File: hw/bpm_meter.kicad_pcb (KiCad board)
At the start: 2 copper layers, 55 x 73.5 mm, 78 parts, among them J1 Conn_01x05_Pin, J2 Conn_01x03_Pin, J901 USB_C_Receptacle_USB2.0, Q1 AO3400A, SW901 SW_MEC_5E, U1 SLS0391FR1A1GD, U2 AOZ1282CI, U3 H11L1, U4 SLS0391FR1A1GD, U5 SLS0391FR1A1GD, U6 LP5030, U7 AMS1117-3.3, U901 RP2040, U902 AMS1117-3.3, U903 W25Q128JVS, Y901 Crystal_GND24_Small

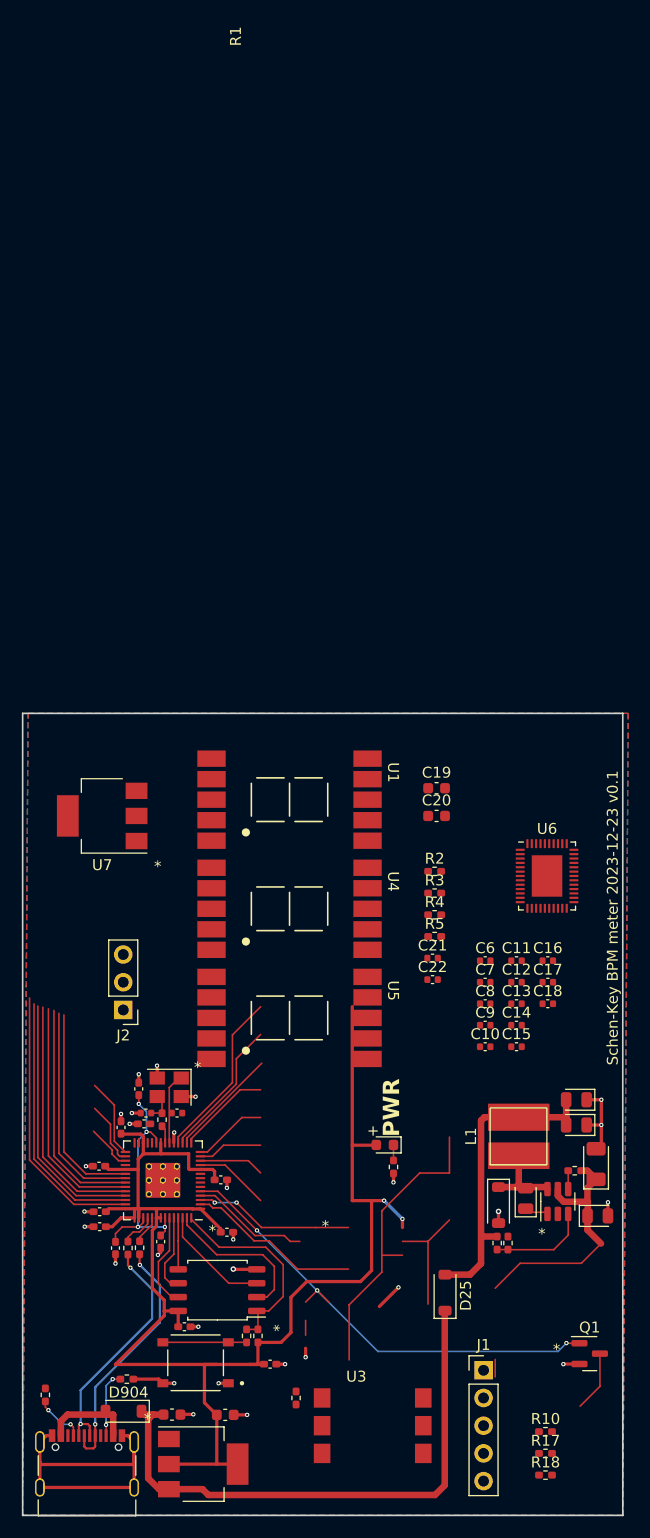
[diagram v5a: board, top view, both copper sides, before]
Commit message: Removed unused tracks, did some prearrangement of components
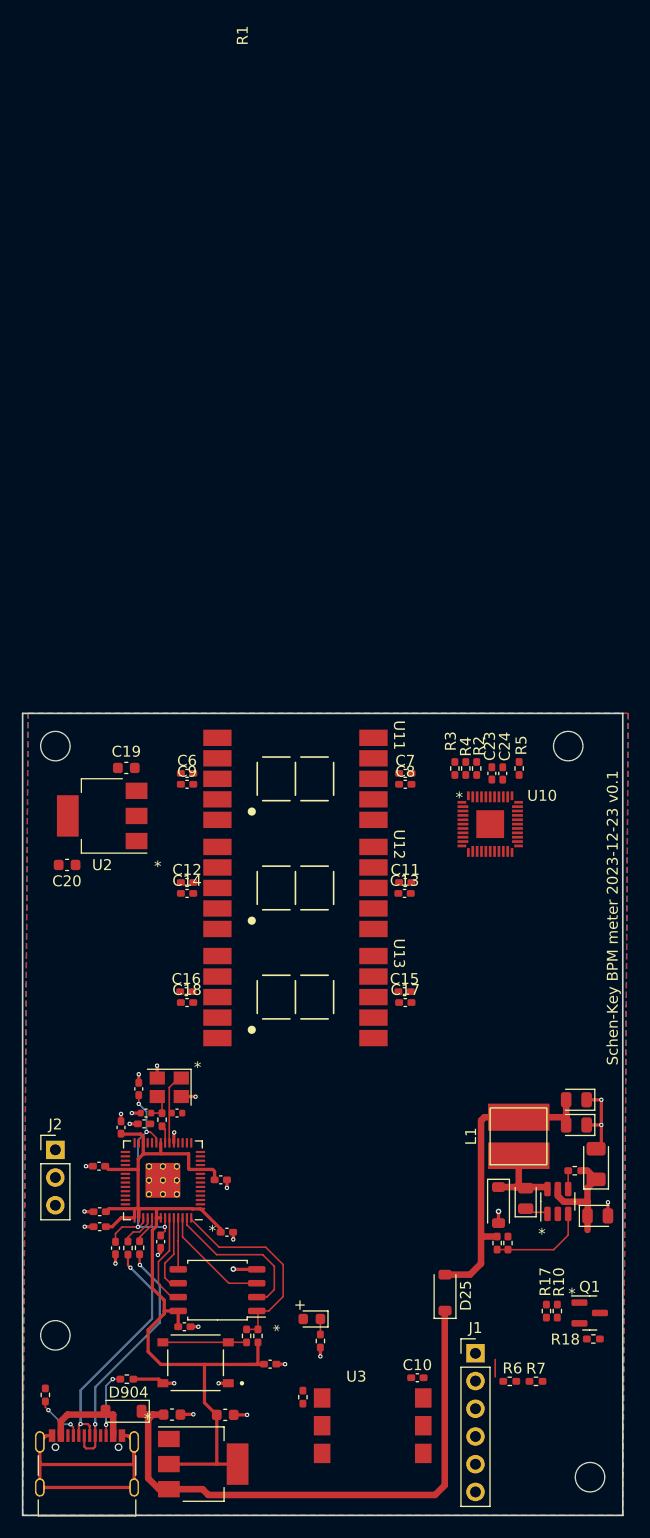
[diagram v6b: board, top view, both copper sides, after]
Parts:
- removed C21, C22: 1u, Capacitor_SMD:C_0402_1005Metric
- removed U6: LP5030, Package_DFN_QFN:VQFN-46-1EP_5x6mm_P0.4mm_EP2.8x3.8mm
- added C23: 1u, Capacitor_SMD:C_0402_1005Metric_Pad0.74x0.62mm_HandSolder, F.Cu at (117.0, 64.5)
- added C24: 100n, Capacitor_SMD:C_0402_1005Metric_Pad0.74x0.62mm_HandSolder, F.Cu at (118.0, 64.5)
- added H1: MountingHole, MountingHole:MountingHole_2.7mm_M2.5, F.Cu at (77.0, 62.0)
- added H2: MountingHole, MountingHole:MountingHole_2.7mm_M2.5, F.Cu at (124.0, 62.0)
- added H3: MountingHole, MountingHole:MountingHole_2.7mm_M2.5, F.Cu at (126.0, 129.0)
- added H4: MountingHole, MountingHole:MountingHole_2.7mm_M2.5, F.Cu at (77.0, 116.0)
- added R6: 10k, Resistor_SMD:R_0402_1005Metric_Pad0.72x0.64mm_HandSolder, F.Cu at (118.6, 120.2)
- added R7: 4k7, Resistor_SMD:R_0402_1005Metric_Pad0.72x0.64mm_HandSolder, F.Cu at (121.0, 120.2)
- added U10: IS31FL3236A, 00_project_library:QFN-44-5x5mm_P0.4mm, F.Cu at (116.8, 69.2)
- C10, C11, C12, C13, C14, C15, C16, C17, C18, C6, C7, C8, C9: footprint Capacitor_SMD:C_0402_1005Metric -> Capacitor_SMD:C_0402_1005Metric_Pad0.74x0.62mm_HandSolder
- J1: value Conn_01x05_Pin -> Conn_01x06_Pin; footprint Connector_PinHeader_2.54mm:PinHeader_1x05_P2.54mm_Vertical -> Connector_PinHeader_2.54mm:PinHeader_1x06_P2.54mm_Vertical
- R2: value 4k7 -> 7k5
- R5: value 4k7 -> 100k
- R901, R902: value 5.1K -> 5.1k
- R906: value 1K -> 1k
- R907: value 10K -> 10k
- moved C9 35.1 mm to (89.1, 65.5)
- moved C20 34.2 mm to (78.1, 72.9)
- moved C16 33.3 mm to (89.0, 84.5)
- moved C18 33.1 mm to (89.1, 85.5)
- moved C14 32.5 mm to (89.1, 75.5)
- moved C6 32.3 mm to (89.1, 64.5)
- moved C12 31.5 mm to (89.1, 74.5)
- moved C10 31.0 mm to (110.2, 119.9)
- moved C19 28.5 mm to (83.5, 64.0), turned to 180 degrees
- moved C8 21.4 mm to (109.1, 65.5)
- moved C7 20.5 mm to (109.1, 64.5)
- moved D901 17.3 mm to (100.5, 114.5)
- moved R905 17.3 mm to (101.3, 116.5)
- moved R5 17.2 mm to (119.5, 64.0), turned to 90 degrees
- moved C13 14.4 mm to (109.0, 75.5)
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- renumbered U2 to U1, U1 to U11, U4 to U12, U5 to U13, U7 to U2
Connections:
- net en renamed sdb
- J1 pad 5: GND -> Net-(J1-Pin_5)
- R1 pad 2: Net-(J1-Pin_3) -> Net-(J1-Pin_4)
- R17 pad 2: Net-(J1-Pin_2) -> Net-(J1-Pin_3)
- U3 pad 2: Net-(J1-Pin_4) -> Net-(J1-Pin_5)
- U901 pad 15: Net-(J2-Pin_1) -> unconnected-(U901-GPIO12-Pad15)
- U901 pad 16: Net-(J2-Pin_2) -> unconnected-(U901-GPIO13-Pad16)
- U901 pad 17: Net-(J2-Pin_3) -> unconnected-(U901-GPIO14-Pad17)
- U901 pad 38: unconnected-(U901-GPIO26/ADC0-Pad38) -> beat_adc
- U901 pad 39: unconnected-(U901-GPIO27/ADC1-Pad39) -> Net-(J2-Pin_1)
- U901 pad 40: unconnected-(U901-GPIO28/ADC2-Pad40) -> Net-(J2-Pin_2)
- U901 pad 41: unconnected-(U901-GPIO29/ADC3-Pad41) -> Net-(J2-Pin_3)
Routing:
- net +3V3: track 138.8 -> 85.4 mm, vias 2 -> 0
- net Net-(Q1-G): track 44.2 -> 0.00 mm, vias 3 -> 0
- net (no net): track 39.9 -> 0.00 mm
- net beat_od: track 26.5 -> 0.00 mm
- net unconnected-(U901-GPIO29/ADC3-Pad41): track 25.3 -> 0.00 mm
- net unconnected-(U901-GPIO28/ADC2-Pad40): track 24.2 -> 0.00 mm
- net unconnected-(U901-GPIO27/ADC1-Pad39): track 23.3 -> 0.00 mm
- net unconnected-(U901-GPIO26/ADC0-Pad38): track 22.6 -> 0.00 mm
- net beat_opto: track 21.7 -> 0.00 mm
- net unconnected-(U901-GPIO23-Pad35): track 19.9 -> 0.00 mm
- net unconnected-(U901-GPIO22-Pad34): track 19.0 -> 0.00 mm
- net sda: track 16.0 -> 0.00 mm
- net unconnected-(U901-GPIO15-Pad18): track 15.6 -> 0.00 mm
- net scl: track 14.6 -> 0.00 mm, vias 2 -> 0
- net +14V: track 25.0 -> 11.8 mm
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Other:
- board text removed: "PWR"

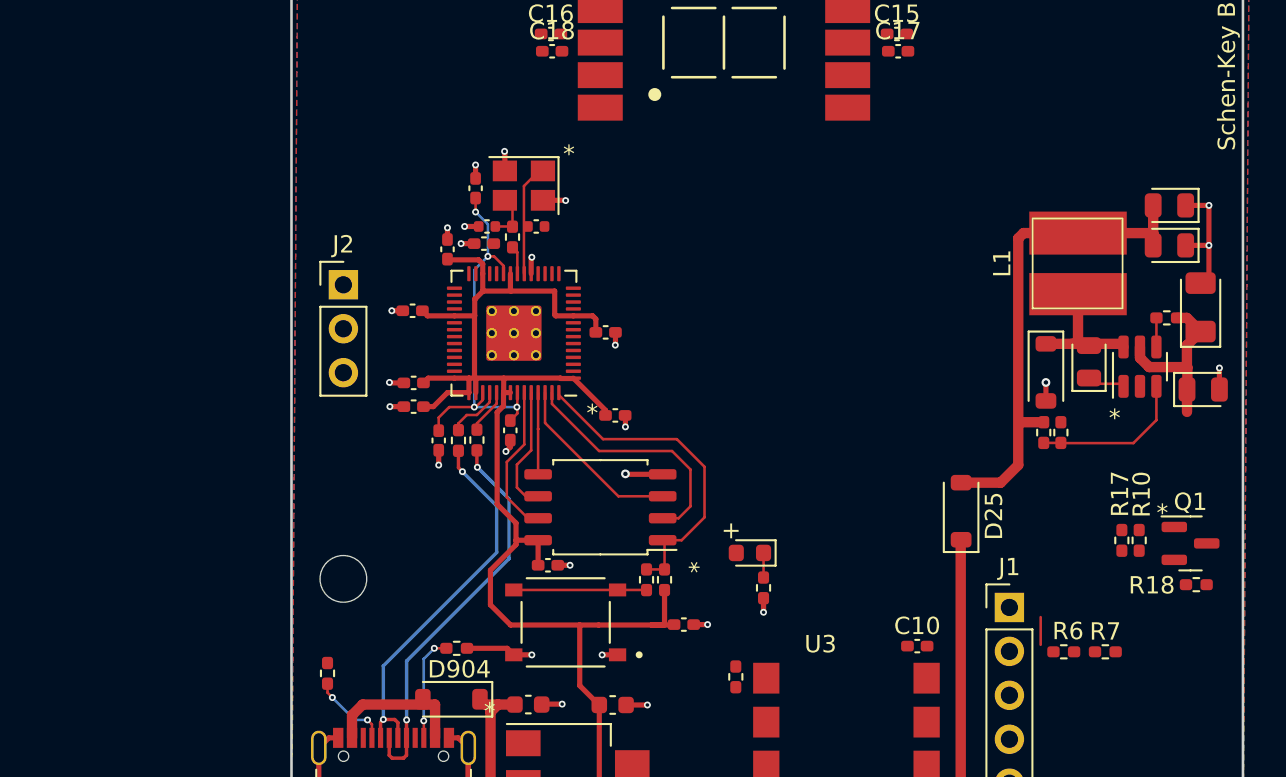
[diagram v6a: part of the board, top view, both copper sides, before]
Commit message: Optimized layout of the RP2040
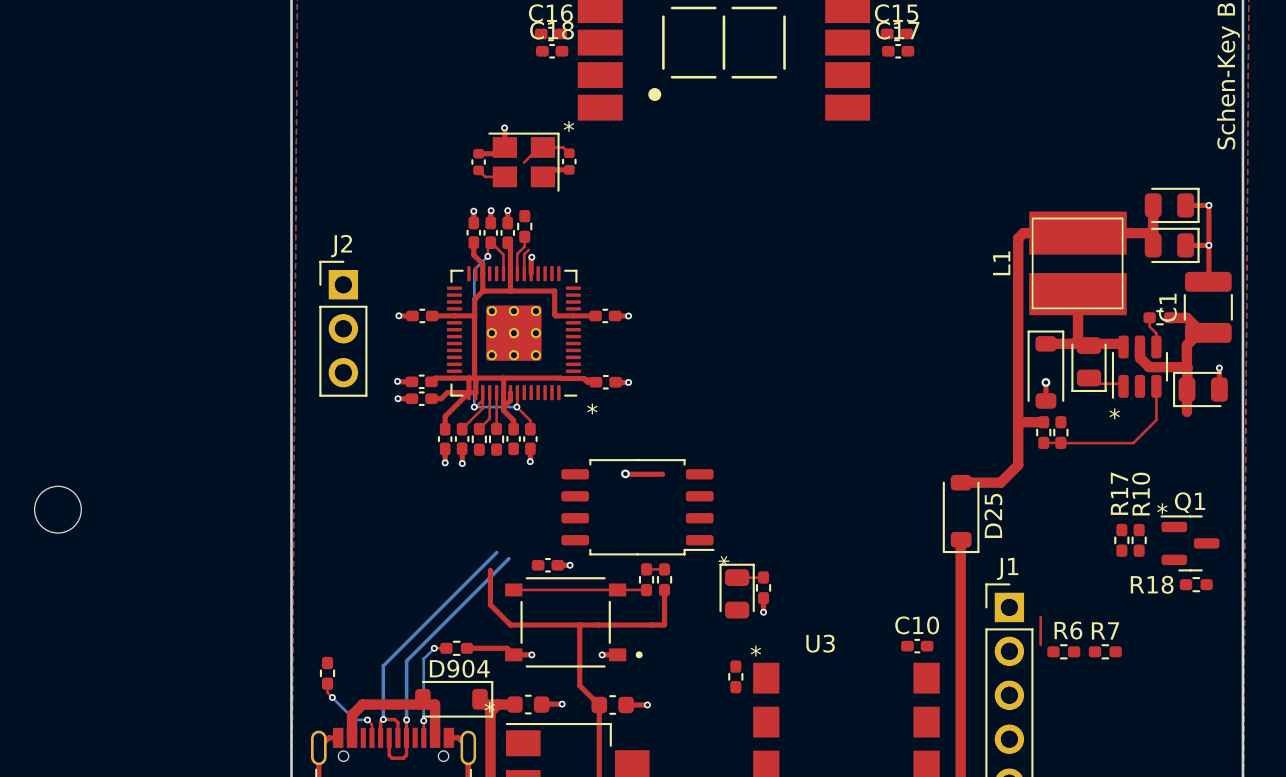
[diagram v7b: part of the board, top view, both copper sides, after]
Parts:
- added C917: 100n, Capacitor_SMD:C_0402_1005Metric_Pad0.74x0.62mm_HandSolder, F.Cu at (86.8, 107.9)
- C1: footprint Diode_SMD:D_1206_3216Metric -> Capacitor_SMD:C_1210_3225Metric
- D901: footprint 00_project_library:LED_0603_1608Metric -> LED_SMD:LED_0805_2012Metric
- moved C906 17.5 mm to (82.9, 107.9), turned to -90 degrees
- moved H4 17.0 mm to (60.5, 112.0)
- moved C905 14.5 mm to (83.9, 107.9), turned to -90 degrees
- moved C904 12.4 mm to (85.5, 96.0), turned to 90 degrees
- moved C909 4.21 mm to (90.1, 91.9), turned to -90 degrees
- moved C910 3.76 mm to (84.8, 91.9), turned to 90 degrees
- moved D901 2.48 mm to (99.8, 116.9), turned to -90 degrees
- moved U903 2.14 mm to (94.0, 111.9)
- moved C916 2.00 mm to (92.2, 104.6)
- moved C907 1.80 mm to (84.5, 96.0)
- moved C908 1.51 mm to (86.5, 96.0), turned to 90 degrees
- moved Y901 1.35 mm to (87.4, 91.9)
- moved C903 1.27 mm to (87.8, 107.9)
- moved R904 1.21 mm to (84.9, 107.9)
- moved R903 1.14 mm to (85.9, 107.9)
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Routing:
- net /cpu/QSPI_SS: track 18.6 -> 1.04 mm
- net /cpu/QSPI_SD1: track 14.3 -> 0.00 mm
- net +3V3: track 85.4 -> 73.7 mm
- net /cpu/QSPI_SD2: track 10.3 -> 0.00 mm
- net /cpu/QSPI_SD3: track 8.18 -> 0.00 mm
- net /cpu/USB_D+: track 23.0 -> 16.0 mm, vias 2 -> 1
- net /cpu/USB_D-: track 22.1 -> 15.3 mm, vias 2 -> 1
- net /cpu/QSPI_SCLK: track 6.54 -> 0.00 mm
- net /cpu/QSPI_SD0: track 4.73 -> 0.00 mm
- net +1V1: track 22.7 -> 20.7 mm, vias 4 -> 3
- net /cpu/XIN: track 6.28 -> 4.46 mm
- net GND: track 63.7 -> 65.1 mm, vias 26 -> 24
- net Net-(U901-USB-DM): track 3.26 -> 2.35 mm
- net /cpu/XOUT: track 1.64 -> 2.31 mm
- net Net-(U901-USB-DP): track 2.61 -> 2.10 mm
